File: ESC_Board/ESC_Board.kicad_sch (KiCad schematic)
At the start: 61 parts, among them Q1 AO3400A, Q3 SIR182DP, Q4 SIR182DP, Q5 SIR182DP, Q6 SIR182Dp, Q7 SIR182DP, Q8 SIR182DP, U2 STM32F051K8Ux, U3 INA180A1, U4 TPS62153RGTT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

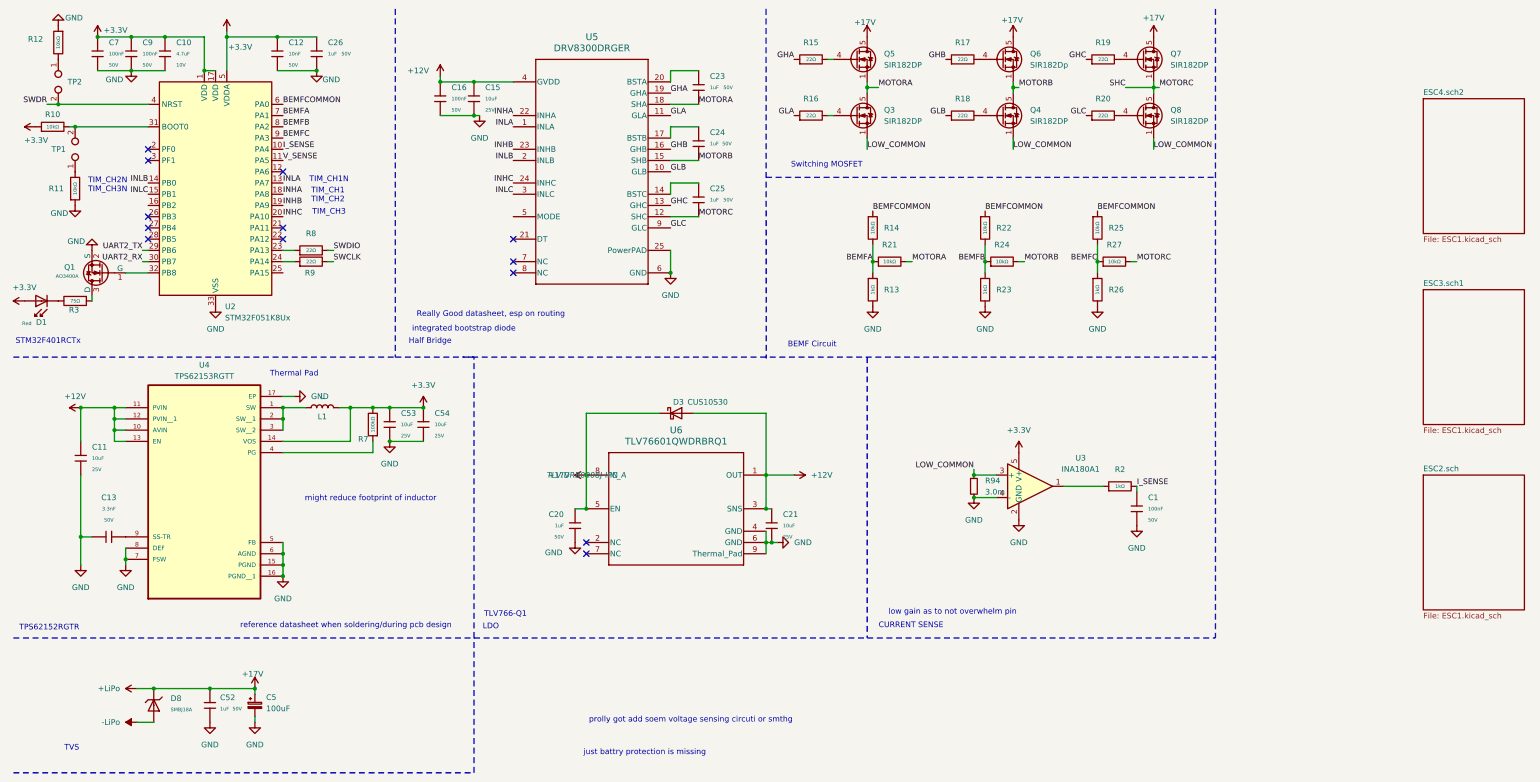
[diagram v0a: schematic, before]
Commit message: DroneController: Adjusted crystal oscillator, added SWD debugging
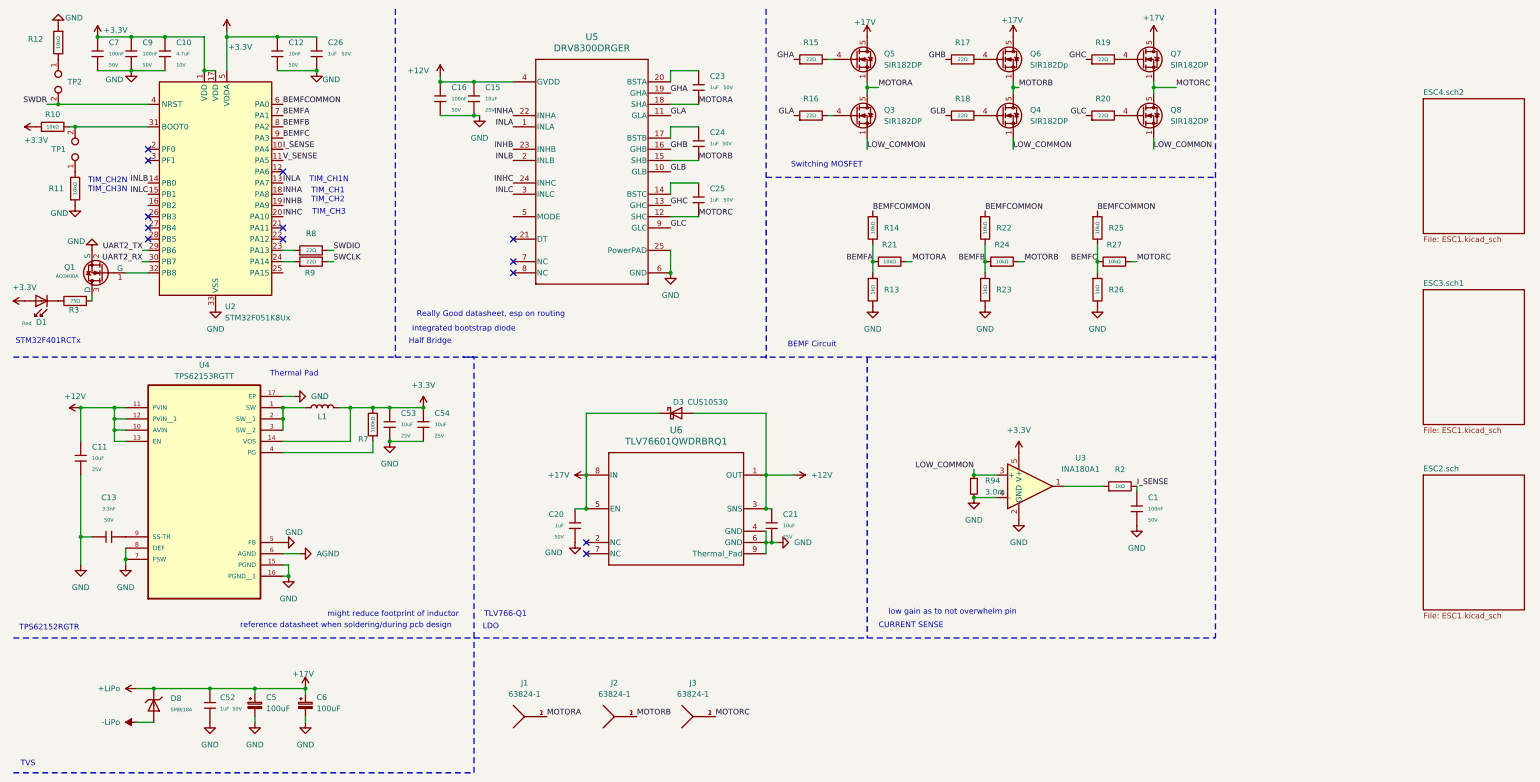
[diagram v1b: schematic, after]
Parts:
- added C6: 100uF, Capacitor_SMD:CP_Elec_8x10, symbol Device:C_Polarized_Small
- added J1, J2, J3: 63824-1, footprints:TRM2_63824-1_TEC, symbol 63824-1:63824-1
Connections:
- net +17V: now also C6.1
- net GND: now also C6.2; no longer U4.6 (AGND)
- net MOTORA: now also J1.1, J1.2
- net MOTORB: now also J2.1, J2.2
- net MOTORC: now also J3.1, J3.2
- new net AGND: U4.6 (AGND)
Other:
- note removed: "just battry protection is missing"
- note removed: "prolly got add soem voltage sensing circuti or smthg"
